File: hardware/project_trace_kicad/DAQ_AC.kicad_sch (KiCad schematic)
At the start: 55 parts, among them U301 THS4131IDR, U303 ADS1602, U304 MCP6499T, U306 LM4040DBZ-4.1

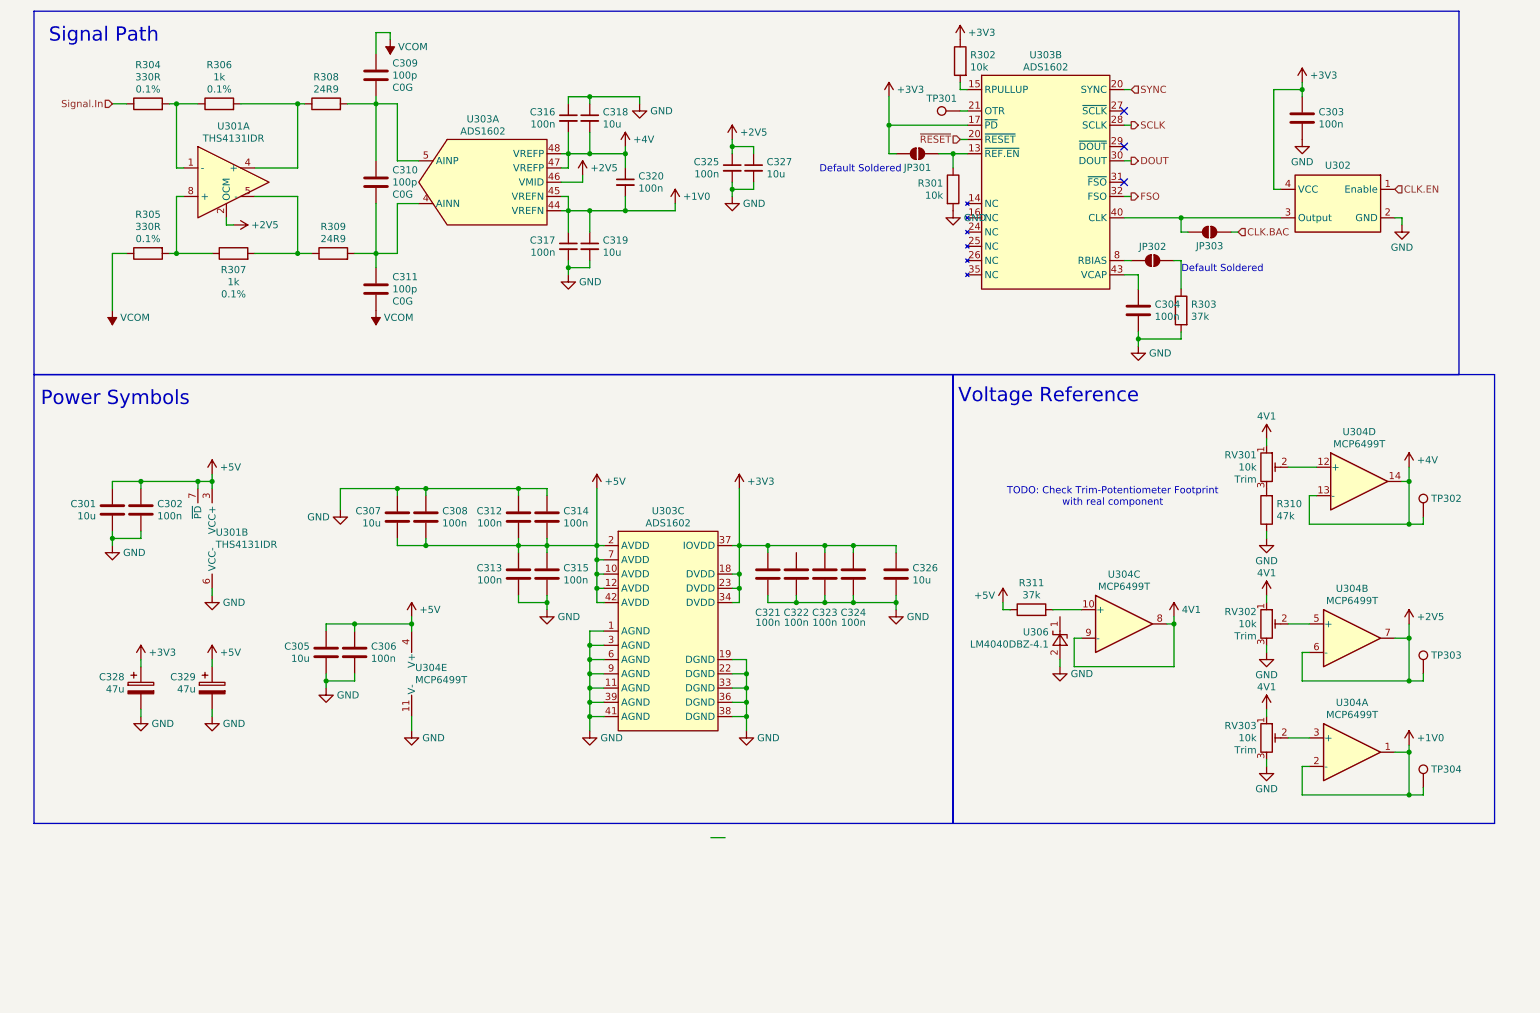
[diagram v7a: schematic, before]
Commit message: ERC Checks & Bug-Fixing
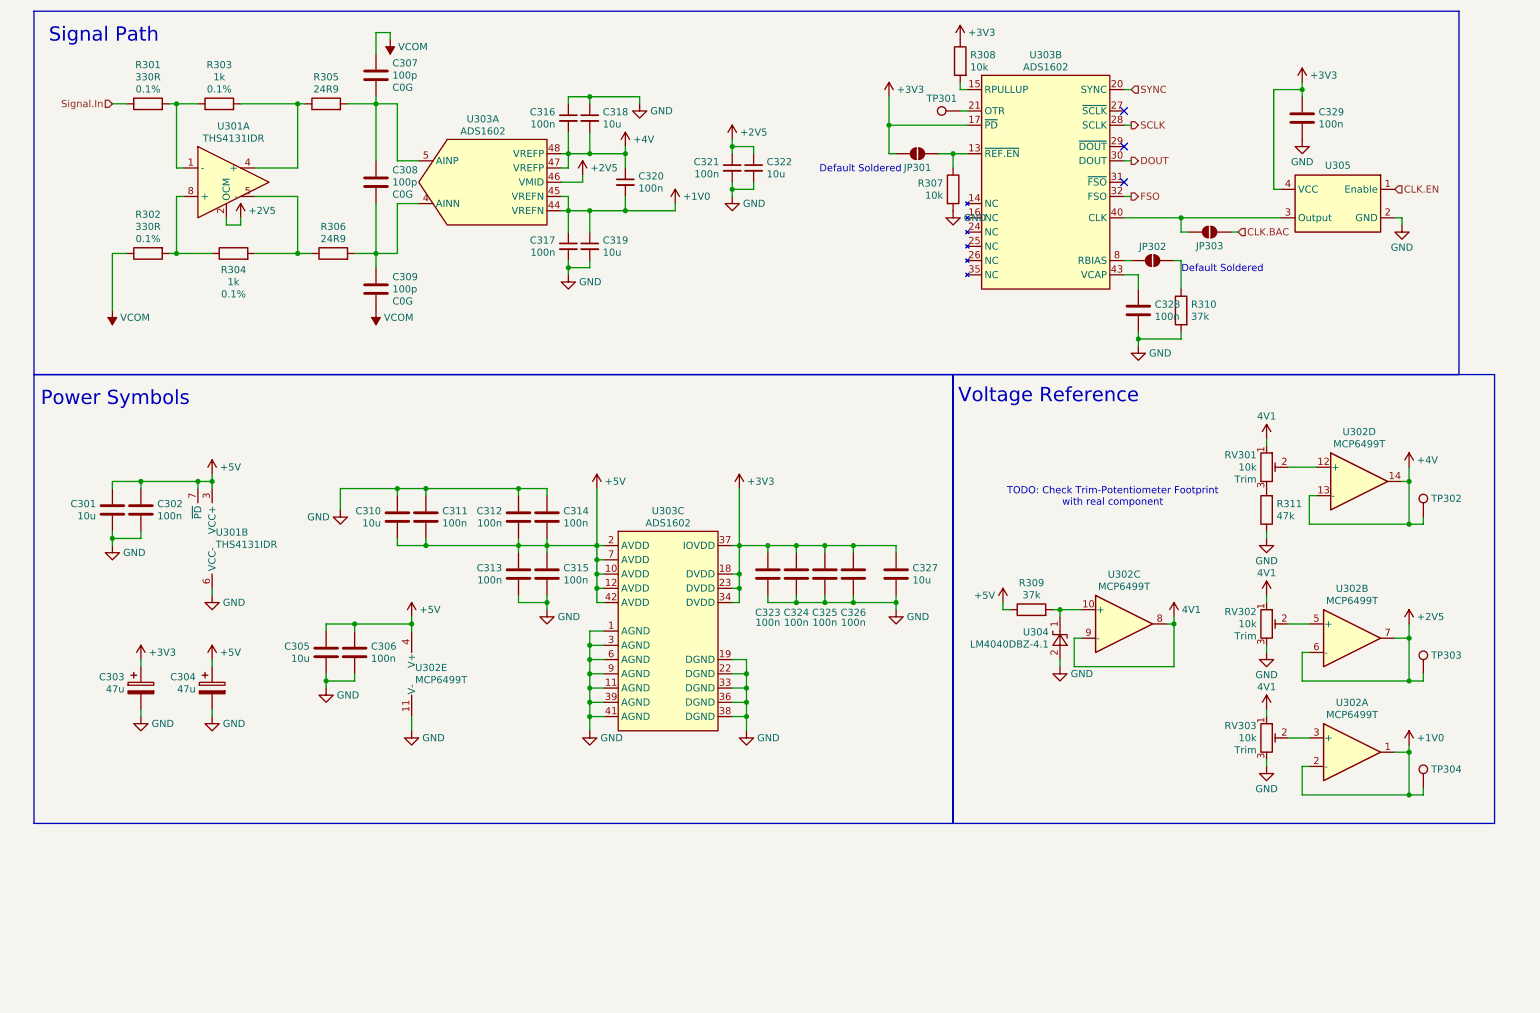
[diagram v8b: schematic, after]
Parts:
- renumbered C328 to C303, C329 to C304, C309 to C307, C310 to C308, C311 to C309, C307 to C310, C308 to C311, C325 to C321, C327 to C322, C321 to C323, C322 to C324, C323 to C325, C324 to C326, C326 to C327, C304 to C328, C303 to C329, R304 to R301, R305 to R302, R306 to R303, R307 to R304, R308 to R305, R309 to R306, R301 to R307, R302 to R308, R311 to R309, R303 to R310, R310 to R311, U304 to U302, U306 to U304, U302 to U305
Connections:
- net ~{RESET} is gone; now on net SYNC: U303.20 (SYNC)
- net +3V3: now also C324.2
- net at U304.1 (K): now also R309.2, U302.10 (+)
